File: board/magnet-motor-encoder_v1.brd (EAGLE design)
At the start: 22 x 22 mm, 12 parts, among them IC1 AS5045B

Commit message: board layout and silkscreen
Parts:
- LED_BLUE: value BLUE -> POWER
- LED_RED: value RED -> DEC
- LED_YELLOW: value YELLOW -> INC
- R1, R2: value 330 -> 1k
- SJ1: value 5V? -> 3V3?
- flipped JP1 to the bottom
- renumbered LED1 to LED_YELLOW, LED2 to LED_RED, LED3 to LED_BLUE
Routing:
- net GND: track 32.0 -> 34.3 mm
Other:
- board text added: "+"
- board text added: "-"
- board text added: "A"
- board text added: "B"
- board text added: "BLUE"
- board text added: "I"
- board text added: "INC DEC POWER"
- board text added: "LEDs 2mA"
- board text added: "Magnet Motor Encoder"
- board text added: "RCA"
- board text added: "RED"
- board text added: "Raphael Lehmann 2016"
- board text added: "Solder"
- board text added: "YELLOW"
- board text added: "for 3V3"
- board text added: "low current"
- board text added: "v1"

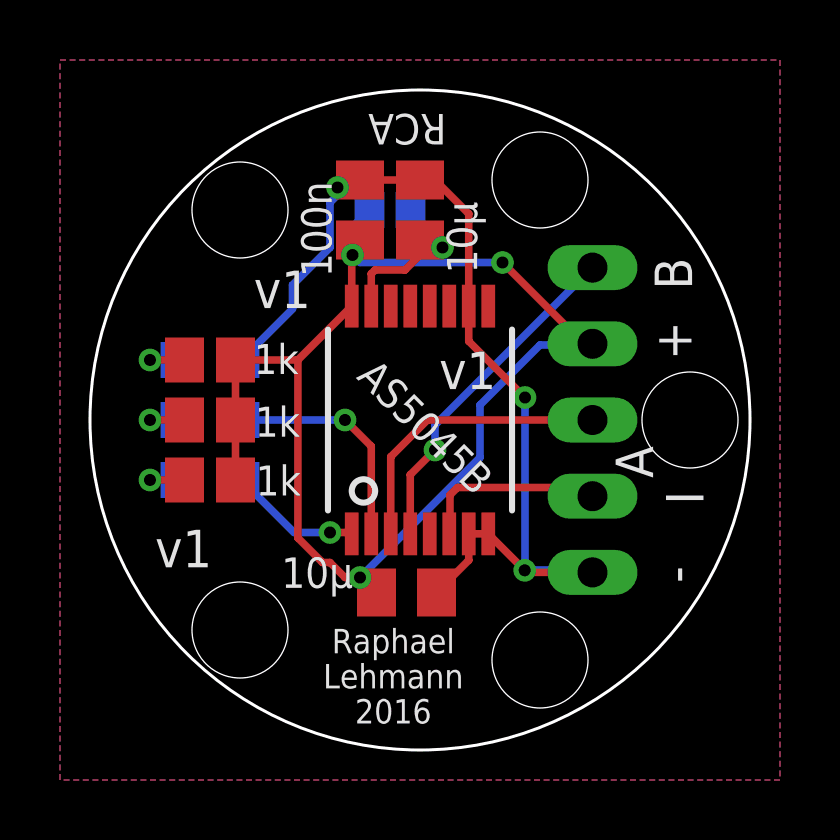
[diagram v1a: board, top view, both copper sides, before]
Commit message: board: silkscreen and ground vias
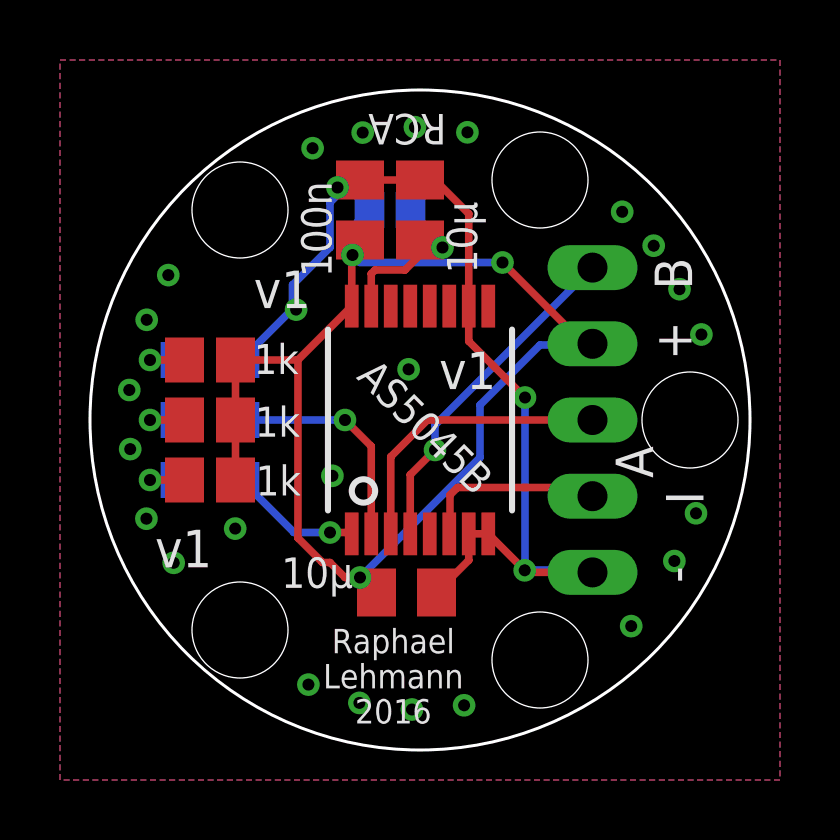
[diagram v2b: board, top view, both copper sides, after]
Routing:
- net GND: vias 3 -> 28
